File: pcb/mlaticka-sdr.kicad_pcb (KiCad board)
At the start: 4 copper layers, 83 x 27.5 mm, 276 parts, among them J1 SMA, J2 SMA, P1 USB_OTG, P2 JTAG, P3 CLK_EXT, U1 R820T, U2 LTC22xx, U3 93LC56BT, U4 FT232H, U5 ASV-12-EJ-T, U6 10M08SCU169, U7 LP5912-3.3, U8 LP5912-3.3

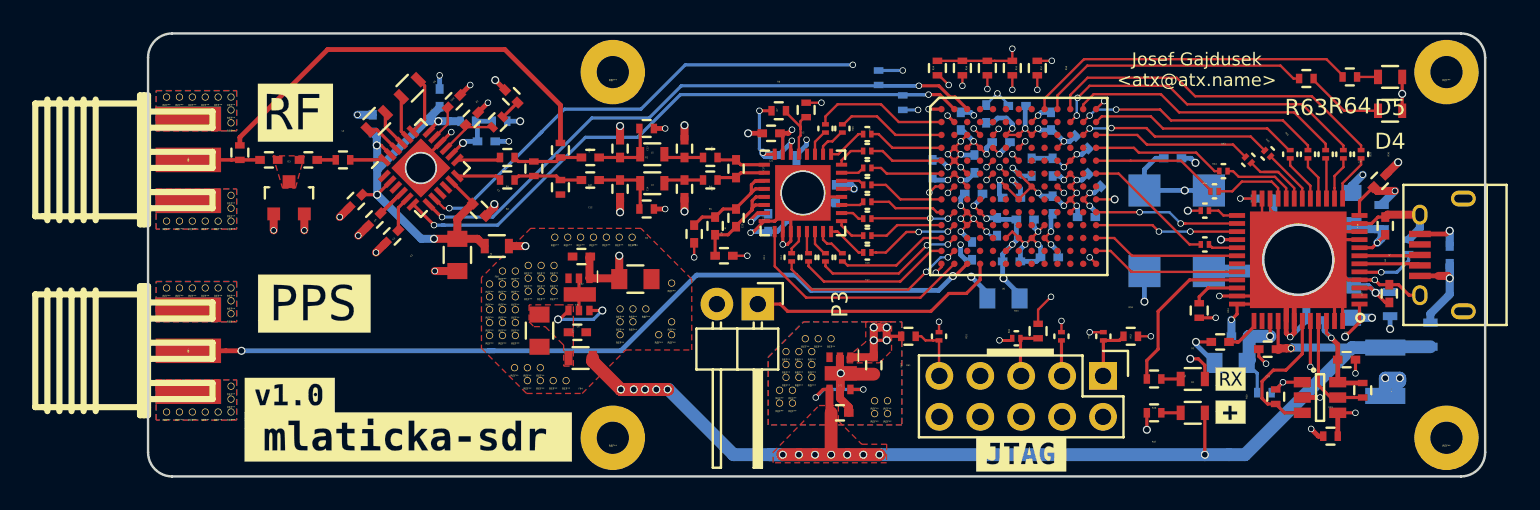
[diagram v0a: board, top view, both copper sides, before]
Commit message: pcb: Update to the v1.1 version
Turns out that I forgot to commit these in the old repository
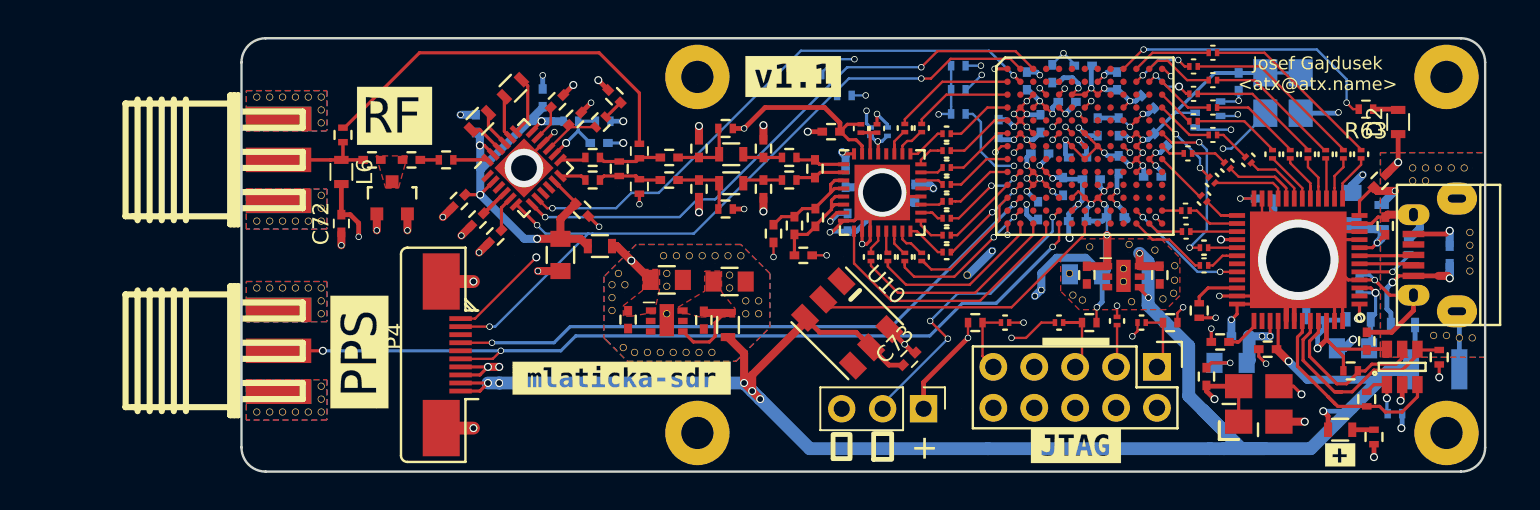
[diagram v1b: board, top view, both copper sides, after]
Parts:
- removed D4, D5: LED, Resistors_SMD:R_0603
- removed the G*** at (79.2, 35.5)
- removed R64: R, Resistors_SMD:R_0402
- removed the REF** at (34.8, 30.4)
- removed the REF** at (34.0, 30.4)
- removed the REF** at (33.2, 30.4)
- removed the REF** at (34.8, 29.6)
- removed the REF** at (34.0, 29.6)
- removed the REF** at (33.2, 29.6)
- removed the REF** at (57.9, 37.7)
- removed the REF** at (57.1, 37.7)
- removed the REF** at (34.8, 28.9)
- removed the REF** at (57.1, 36.9)
- removed the REF** at (57.9, 36.9)
- removed the REF** at (54.4, 33.0)
- removed the REF** at (52.8, 33.0)
- removed the REF** at (53.6, 33.0)
- removed the REF** at (52.0, 36.2)
- removed the REF** at (51.2, 37.0)
- removed the REF** at (51.2, 36.2)
- removed the REF** at (52.0, 37.0)
- removed the REF** at (51.6, 34.6)
- removed the REF** at (34.0, 28.9)
- removed the REF** at (53.2, 34.6)
- removed the REF** at (53.2, 35.5)
- removed the REF** at (52.4, 35.5)
- removed the REF** at (51.6, 35.5)
- removed the REF** at (52.4, 34.6)
- removed the REF** at (53.2, 33.9)
- removed the REF** at (52.4, 33.9)
- removed the REF** at (51.6, 33.9)
- removed the REF** at (42.0, 26.8)
- removed the REF** at (41.2, 26.8)
- removed the REF** at (40.5, 26.8)
- removed the REF** at (39.6, 26.8)
- removed the REF** at (38.9, 26.8)
- removed the REF** at (38.0, 26.8)
- removed the REF** at (37.2, 26.8)
- removed the REF** at (36.4, 28.5)
- removed the REF** at (37.2, 28.5)
- removed the REF** at (35.6, 28.5)
- removed the REF** at (36.4, 34.9)
- removed the REF** at (38.0, 35.6)
- removed the REF** at (37.1, 35.6)
- removed the REF** at (36.4, 35.6)
- removed the REF** at (44.5, 29.6)
- removed the REF** at (44.5, 32.0)
- removed the REF** at (43.7, 32.8)
- removed the REF** at (44.5, 32.8)
- removed the REF** at (42.1, 32.0)
- removed the REF** at (41.3, 32.8)
- removed the REF** at (41.3, 32.0)
- removed the REF** at (41.3, 31.2)
- removed the REF** at (42.9, 31.2)
- removed the REF** at (42.1, 31.2)
- removed the REF** at (35.6, 29.3)
- removed the REF** at (37.2, 29.3)
- removed the REF** at (36.4, 29.3)
- removed the REF** at (36.4, 30.1)
- removed the REF** at (37.2, 30.1)
- removed the REF** at (35.6, 30.1)
- removed the REF** at (35.5, 35.6)
- removed the REF** at (35.5, 34.9)
- removed the REF** at (34.8, 34.9)
- removed the REF** at (34.8, 32.9)
- removed the REF** at (34.0, 32.9)
- removed the REF** at (33.2, 32.9)
- removed the REF** at (34.8, 32.0)
- removed the REF** at (34.0, 32.0)
- removed the REF** at (33.2, 32.0)
- removed the REF** at (34.8, 31.2)
- removed the REF** at (34.0, 31.2)
- removed the REF** at (33.2, 31.2)
- added C71: 100n, Capacitors_SMD:C_0402, B.Cu at (79.7, 17.1)
- added C72: 100n, Capacitors_SMD:C_0402, F.Cu at (24.0, 25.9)
- added C73: 100n, Capacitors_SMD:C_0402, F.Cu at (59.2, 34.3)
- added JP1: JMP_NO, Resistors_SMD:R_0402, F.Cu at (42.5, 21.4)
- added JP2: JMP_NO, Resistors_SMD:R_0402, F.Cu at (42.5, 23.6)
- added L6: 220n, Resistors_SMD:R_0603, F.Cu at (24.0, 22.7)
- added P4: CONN_EXT, footprints:SFV10R, F.Cu at (27.8, 32.9)
- added R65: 33R, Resistors_SMD:R_0201, F.Cu at (76.9, 19.6)
- added R66: 33R, Resistors_SMD:R_0201, F.Cu at (78.1, 18.7)
- added R67: 33R, Resistors_SMD:R_0201, F.Cu at (76.9, 17.9)
- added R68: 33R, Resistors_SMD:R_0201, F.Cu at (78.1, 17.0)
- added R69: 33R, Resistors_SMD:R_0201, F.Cu at (76.9, 16.1)
- added R70: 33R, Resistors_SMD:R_0201, F.Cu at (78.1, 15.3)
- added R71: 33R, Resistors_SMD:R_0201, F.Cu at (76.4, 25.1)
- added R72: 33R, Resistors_SMD:R_0201, F.Cu at (76.4, 26.4)
- added R73: 33R, Resistors_SMD:R_0201, F.Cu at (77.5, 28.5)
- added R74: DNP, Resistors_SMD:R_0201, F.Cu at (57.2, 20.0)
- added REF**: Via, footprints:Via, F.Cu at (75.7, 30.2)
- added REF**: Via, footprints:Via, F.Cu at (90.5, 22.4)
- added REF**: Via, footprints:Via, F.Cu at (94.0, 28.9)
- added REF**: Via, footprints:Via, F.Cu at (94.0, 26.4)
- added REF**: Via, footprints:Via, F.Cu at (94.0, 28.1)
- added REF**: Via, footprints:Via, F.Cu at (94.0, 27.2)
- added REF**: Via, footprints:Via, F.Cu at (93.4, 33.0)
- added REF**: Via, footprints:Via, F.Cu at (94.2, 33.0)
- added REF**: Via, footprints:Via, F.Cu at (91.8, 32.9)
- added REF**: Via, footprints:Via, F.Cu at (92.6, 32.9)
- added REF**: Via, footprints:Via, F.Cu at (62.9, 29.1)
- added REF**: Via, footprints:Via, F.Cu at (75.0, 30.6)
- added REF**: Via, footprints:Via, F.Cu at (49.9, 31.5)
- added REF**: Via, footprints:Via, F.Cu at (49.1, 31.5)
- added REF**: Via, footprints:Via, F.Cu at (49.9, 30.7)
- added REF**: Via, footprints:Via, F.Cu at (49.1, 30.7)
- added REF**: Via, footprints:Via, F.Cu at (48.1, 29.9)
- added REF**: Via, footprints:Via, F.Cu at (48.1, 29.1)
- added REF**: Via, footprints:Via, F.Cu at (44.2, 29.8)
- added REF**: Via, footprints:Via, F.Cu at (44.2, 29.0)
- added REF**: Via, footprints:Via, F.Cu at (48.8, 27.9)
- added REF**: Via, footprints:Via, F.Cu at (48.0, 27.9)
- added REF**: Via, footprints:Via, F.Cu at (75.7, 29.4)
- added REF**: Via, footprints:Via, F.Cu at (47.2, 27.9)
- added REF**: Via, footprints:Via, F.Cu at (46.4, 27.9)
- added REF**: Via, footprints:Via, F.Cu at (45.6, 27.9)
- added REF**: Via, footprints:Via, F.Cu at (44.8, 27.9)
- added REF**: Via, footprints:Via, F.Cu at (44.0, 27.9)
- added REF**: Via, footprints:Via, F.Cu at (41.5, 33.6)
- added REF**: Via, footprints:Via, F.Cu at (41.2, 29.0)
- added REF**: Via, footprints:Via, F.Cu at (41.6, 29.7)
- added REF**: Via, footprints:Via, F.Cu at (40.8, 30.5)
- added REF**: Via, footprints:Via, F.Cu at (40.8, 29.7)
- added REF**: Via, footprints:Via, F.Cu at (90.5, 23.2)
- added REF**: Via, footprints:Via, F.Cu at (40.8, 31.3)
- added REF**: Via, footprints:Via, F.Cu at (44.2, 31.5)
- added REF**: Via, footprints:Via, F.Cu at (47.0, 33.9)
- added REF**: Via, footprints:Via, F.Cu at (46.2, 33.9)
- added REF**: Via, footprints:Via, F.Cu at (45.4, 33.9)
- added REF**: Via, footprints:Via, F.Cu at (44.6, 33.9)
- added REF**: Via, footprints:Via, F.Cu at (43.8, 33.9)
- added REF**: Via, footprints:Via, F.Cu at (43.0, 33.9)
- added REF**: Via, footprints:Via, F.Cu at (42.2, 33.9)
- added REF**: Via, footprints:Via, F.Cu at (70.0, 30.6)
- added REF**: Via, footprints:Via, F.Cu at (91.3, 23.2)
- added REF**: Via, footprints:Via, F.Cu at (69.4, 30.3)
- added REF**: Via, footprints:Via, F.Cu at (69.2, 29.0)
- added REF**: Via, footprints:Via, F.Cu at (75.7, 28.5)
- added REF**: Via, footprints:Via, F.Cu at (70.5, 27.4)
- added REF**: Via, footprints:Via, F.Cu at (72.9, 27.2)
- added REF**: Via, footprints:Via, F.Cu at (74.5, 27.6)
- added REF**: Via, footprints:Via, F.Cu at (73.0, 30.8)
- added REF**: Via, footprints:Via, F.Cu at (72.5, 29.5)
- added REF**: Via, footprints:Via, F.Cu at (72.5, 28.7)
- added REF**: Via, footprints:Via, F.Cu at (93.7, 22.4)
- added REF**: Via, footprints:Via, F.Cu at (92.9, 22.4)
- added REF**: Via, footprints:Via, F.Cu at (92.1, 22.4)
- added REF**: Via, footprints:Via, F.Cu at (91.3, 22.4)
- added U10: WS2812, footprints:WS2812, F.Cu at (55.4, 32.1)
- added U9: ASFL1-30.000MHZ-EK-T, footprints:ABRACON-ASFL1, B.Cu at (82.5, 17.8)
- C31: moved to F.Cu
- C37, R54, R55, R56, R57, R58: moved to B.Cu
- D2: value LED_RX -> LED
- P1: footprint Connect:USB_Micro-B -> footprints:USB_Micro-B
- P3: value CLK_EXT -> CONN_CLK_EXT; footprint Pin_Headers:Pin_Header_Angled_1x02 -> Pin_Headers:Pin_Header_Straight_1x03_Pitch2.54mm
- R12: value 19k -> 20k
- R27: value 0 -> DNP
- R32, R33: value 0 -> 33R; footprint Resistors_SMD:R_0402 -> Resistors_SMD:R_0201
- R48: value R -> 0; footprint Resistors_SMD:R_0402 -> Resistors_SMD:R_0201
- R6, R7: footprint Resistors_SMD:R_0402 -> Resistors_SMD:R_0201; moved to B.Cu
- U5: value ASV-12-EJ-T -> ASFL1-12.000MHZ-EK-T; footprint footprints:ASV-XX -> footprints:ABRACON-ASFL1; moved to F.Cu
- moved R33 40.6 mm to (78.1, 20.4), turned to 180 degrees
- moved R32 39.0 mm to (76.5, 21.6), turned to 180 degrees
- moved G*** 37.0 mm to (52.0, 16.8)
- moved R48 23.9 mm to (56.2, 20.0), turned to 270 degrees
- moved C42 21.6 mm to (74.8, 29.1), turned to 270 degrees
- moved D2 20.4 mm to (89.6, 19.6), turned to 90 degrees
- moved U7 18.6 mm to (72.5, 29.2), turned to 90 degrees
- moved C47 14.4 mm to (70.3, 29.1)
- moved G*** 13.7 mm to (41.4, 35.5)
- moved R47 13.7 mm to (88.1, 39.1), turned to 270 degrees
- moved C31 13.7 mm to (77.7, 35.4), turned to 90 degrees
- moved C50 12.2 mm to (48.1, 29.5), turned to 0 degrees
- moved P3 12.2 mm to (60.1, 37.4)
- moved U5 11.8 mm to (80.9, 37.1), turned to 0 degrees
- moved R57 11.8 mm to (77.0, 19.5)
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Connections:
- D2 pad 1: Net-(D2-Pad1) -> GND
- D2 pad 2: /FTDI/3.3V_FT -> Net-(D2-Pad2)
- P3 pad 1: /FPGA/CLK_EXT -> 3.3V_FPGA
- P3 pad 2: GND -> /FPGA/CLK_EXT
- R32 pad 1: /ADC/BYPASS -> /FTDI/D7
- R32 pad 2: /RF/IF_P -> /FPGA/FT_D7
- R33 pad 1: /RF/IF_N -> /FTDI/D6
- R33 pad 2: (no net) -> /FPGA/FT_D6
- R48 pad 1: Net-(D2-Pad1) -> /ADC/VCM
- R48 pad 2: /FTDI/LED_RX -> Net-(R48-Pad2)
- R63 pad 1: Net-(D4-Pad2) -> Net-(D2-Pad2)
- U2 pad 30: 3.3V_A -> Net-(R48-Pad2)
- U4 pad 1: /FPGA/12MHz -> /FTDI/12MHz
- U4 pad 33: /FTDI/LED_RX -> (no net)
- U5 pad 3: /FPGA/12MHz -> /FTDI/12MHz
- U6 pad A11: /FTDI/D0 -> /FPGA/FT_D0
- U6 pad A12: /FTDI/D2 -> /FPGA/FT_D2
- U6 pad A9: Net-(R64-Pad2) -> (no net)
- U6 pad B11: /FTDI/D1 -> /FPGA/FT_D1
- U6 pad B12: /FTDI/D3 -> /FPGA/FT_D3
- U6 pad B13: /FTDI/D4 -> /FPGA/FT_D4
- U6 pad C12: /FTDI/D5 -> (no net)
- U6 pad C13: /FTDI/D6 -> /FPGA/FT_D5
- U6 pad D13: /FTDI/D7 -> /FPGA/FT_D6
- U6 pad G10: /FPGA/12MHz -> /FPGA/30Mhz
- U6 pad G13: (no net) -> /FPGA/FT_D7
- U6 pad J13: /FPGA/FT_~RD -> (no net)
- U6 pad K13: /FPGA/FT_~WR -> (no net)
- U6 pad L13: /FPGA/FT_~OE -> (no net)
- U6 pad L2: /FPGA/ADC_D2 -> /FPGA/EXT_P1
- U6 pad M1: /FPGA/ADC_D1 -> (no net)
- U6 pad M11: (no net) -> /FPGA/FT_RST
- U6 pad M13: /FPGA/FT_RST -> Net-(R71-Pad2)
- U6 pad M2: /FPGA/ADC_D0 -> /FPGA/ADC_D2
- U6 pad M5: (no net) -> /FPGA/CLK_EXT
- U6 pad N11: (no net) -> Net-(R73-Pad2)
- U6 pad N12: (no net) -> Net-(R72-Pad2)
- U6 pad N2: /FPGA/ADC_CLK -> /FPGA/ADC_D1
- U6 pad N3: /FPGA/PPS -> /FPGA/ADC_D0
- U6 pad N4: /FPGA/CLK_EXT -> /FPGA/ADC_CLK
- U6 pad N5: (no net) -> /FPGA/PPS
- U6 pad N7: (no net) -> /FPGA/LED_DATA
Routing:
- net +5V: track 88.9 -> 138.8 mm, vias 17 -> 10
- net 3.3V_FPGA: track 70.2 -> 114.8 mm
- net /FPGA/EXT_P1: track 0.00 -> 38.5 mm, vias 0 -> 2
- net /FPGA/12MHz: track 27.5 -> 0.00 mm, vias 3 -> 0
- net Net-(R64-Pad2): track 20.7 -> 0.00 mm
- net /FPGA/LED_DATA: track 0.00 -> 19.0 mm
- net /FTDI/3.3V_FT: track 34.4 -> 51.0 mm
- net /FPGA/30Mhz: track 0.00 -> 13.4 mm, vias 0 -> 2
- net /FTDI/LED_RX: track 10.2 -> 0.00 mm
- net /FTDI/D0: track 21.4 -> 11.5 mm
- net /FTDI/12MHz: track 0.00 -> 9.51 mm, vias 0 -> 2
- net /FTDI/D1: track 20.3 -> 11.2 mm, vias 2 -> 0
- net /FTDI/D2: track 17.3 -> 8.54 mm
- net /FPGA/SCL: track 39.7 -> 47.6 mm, vias 2 -> 3
- net /FTDI/D6: track 9.84 -> 2.33 mm
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- added copper zone on F.Cu, net 3.3V_A
- removed copper zone on F.Cu, net +5V
- removed copper zone on F.Cu, net 3.3V_FPGA
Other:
- board size 83 x 27.5 mm -> 77.2 x 26.9 mm
- board text added: "+"
- board text added: "⌚"
- board text added: "⏚"
